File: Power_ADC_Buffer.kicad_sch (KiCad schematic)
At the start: 36 parts, among them U6 TLV6001DCK, U7 TLV6001DCK, U8 TLV6001DCK, U9 TLV6001DCK

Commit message: Adjusted cap sizes, 0603 for all need hand soldering, 0402 where possible, 0804 as needed
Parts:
- C20, C21, C22, C23, C24, C25, C26, C27: footprint Capacitor_SMD:C_0402_1005Metric_Pad0.74x0.62mm_HandSolder -> Capacitor_SMD:C_0603_1608Metric
- R12, R13, R14, R15, R16, R17, R18, R19, R20, R21, R22, R23, R24, R25, R26, R27, R28, R29, R30, R31: footprint Resistor_SMD:R_0402_1005Metric_Pad0.72x0.64mm_HandSolder -> Resistor_SMD:R_0603_1608Metric

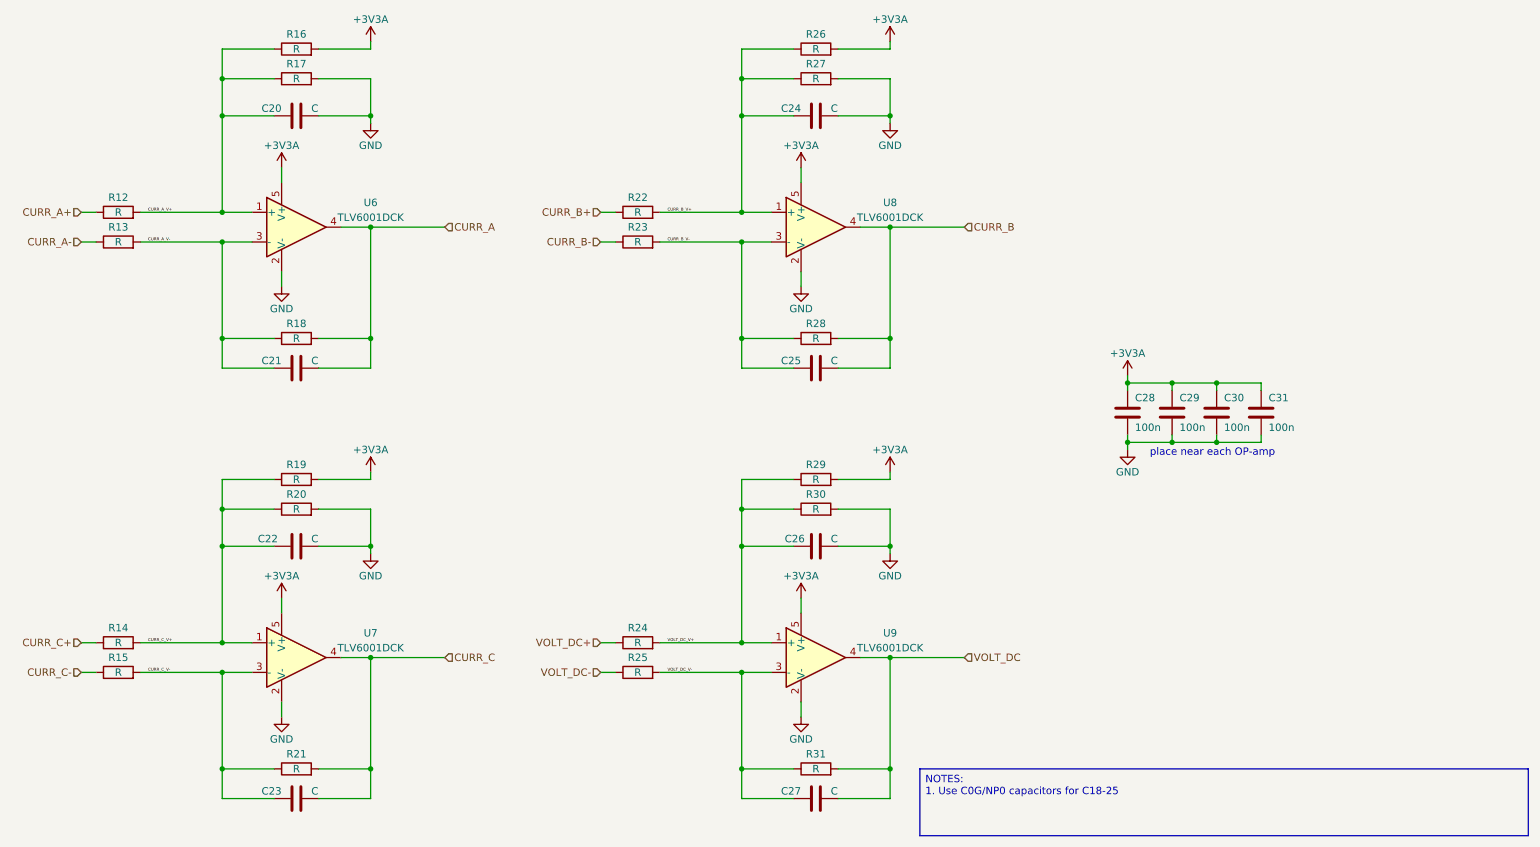
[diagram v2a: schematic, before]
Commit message: Changed op Amp, need to reroute, need to re-asses capacitor situation since || 0.1 and 1 is dumb. Just use 2 1s in that case.
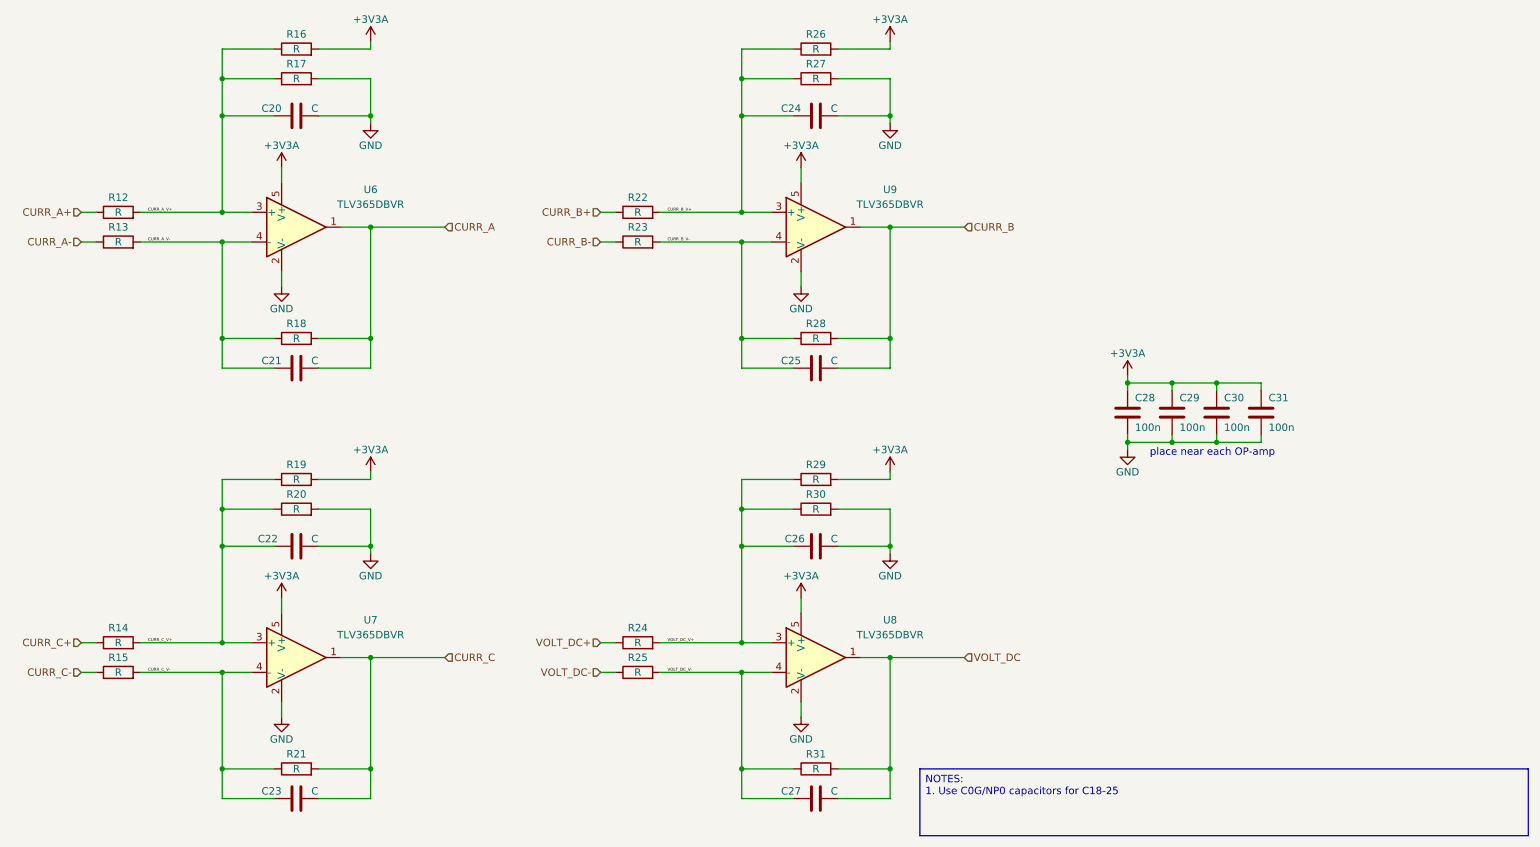
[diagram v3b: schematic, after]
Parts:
- removed U6, U7, U8, U9: TLV6001DCK, Package_TO_SOT_SMD:SOT-353_SC-70-5, symbol Amplifier_Operational:TLV6001DCK
- added U6, U7, U8, U9: TLV365DBVR, Package_TO_SOT_SMD:SOT-23-5, symbol User_OpAmp:TLV365DBVR
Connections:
- net +3V3A: now also U6.5 (V+), U7.5 (V+), U8.5 (V+), U9.5 (V+)
- net CURR_A: now also U6.1
- net CURR_A_V+: now also U6.3 (+)
- net CURR_A_V-: now also U6.4 (-)
- net CURR_B: now also U9.1
- net CURR_B_V+: now also U9.3 (+)
- net CURR_B_V-: now also U9.4 (-)
- net CURR_C: now also U7.1
- net CURR_C_V+: now also U7.3 (+)
- net CURR_C_V-: now also U7.4 (-)
- net GND: now also U6.2 (V-), U7.2 (V-), U8.2 (V-), U9.2 (V-)
- net VOLT_DC: now also U8.1
- net VOLT_DC_V+: now also U8.3 (+)
- net VOLT_DC_V-: now also U8.4 (-)

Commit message: Cheaper, smaller 10MHz Op Amp
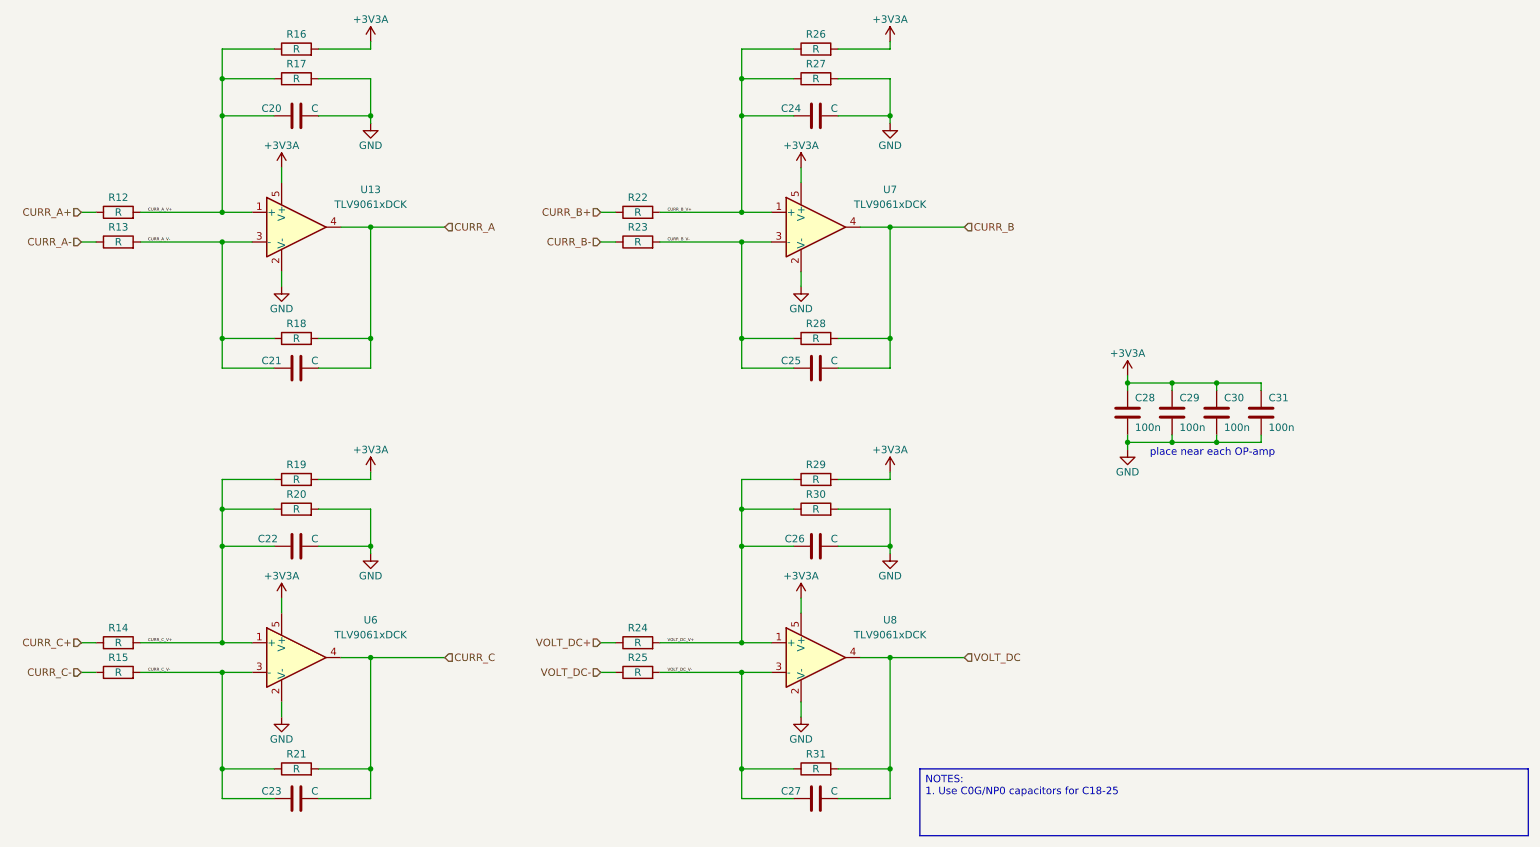
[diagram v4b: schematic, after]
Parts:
- removed U6, U7, U8, U9: TLV365DBVR, Package_TO_SOT_SMD:SOT-23-5, symbol User_OpAmp:TLV365DBVR
- added U13, U6, U7, U8: TLV9061xDCK, Package_TO_SOT_SMD:SOT-353_SC-70-5, symbol Amplifier_Operational:TLV9061xDCK
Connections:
- net +3V3A: now also U13.5 (V+), U6.5 (V+), U7.5 (V+), U8.5 (V+)
- net CURR_A: now also U13.4
- net CURR_A_V+: now also U13.1 (+)
- net CURR_A_V-: now also U13.3 (-)
- net CURR_B: now also U7.4
- net CURR_B_V+: now also U7.1 (+)
- net CURR_B_V-: now also U7.3 (-)
- net CURR_C: now also U6.4
- net CURR_C_V+: now also U6.1 (+)
- net CURR_C_V-: now also U6.3 (-)
- net GND: now also U13.2 (V-), U6.2 (V-), U7.2 (V-), U8.2 (V-)
- net VOLT_DC: now also U8.4
- net VOLT_DC_V+: now also U8.1 (+)
- net VOLT_DC_V-: now also U8.3 (-)

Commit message: Updating all decoupling to 1u
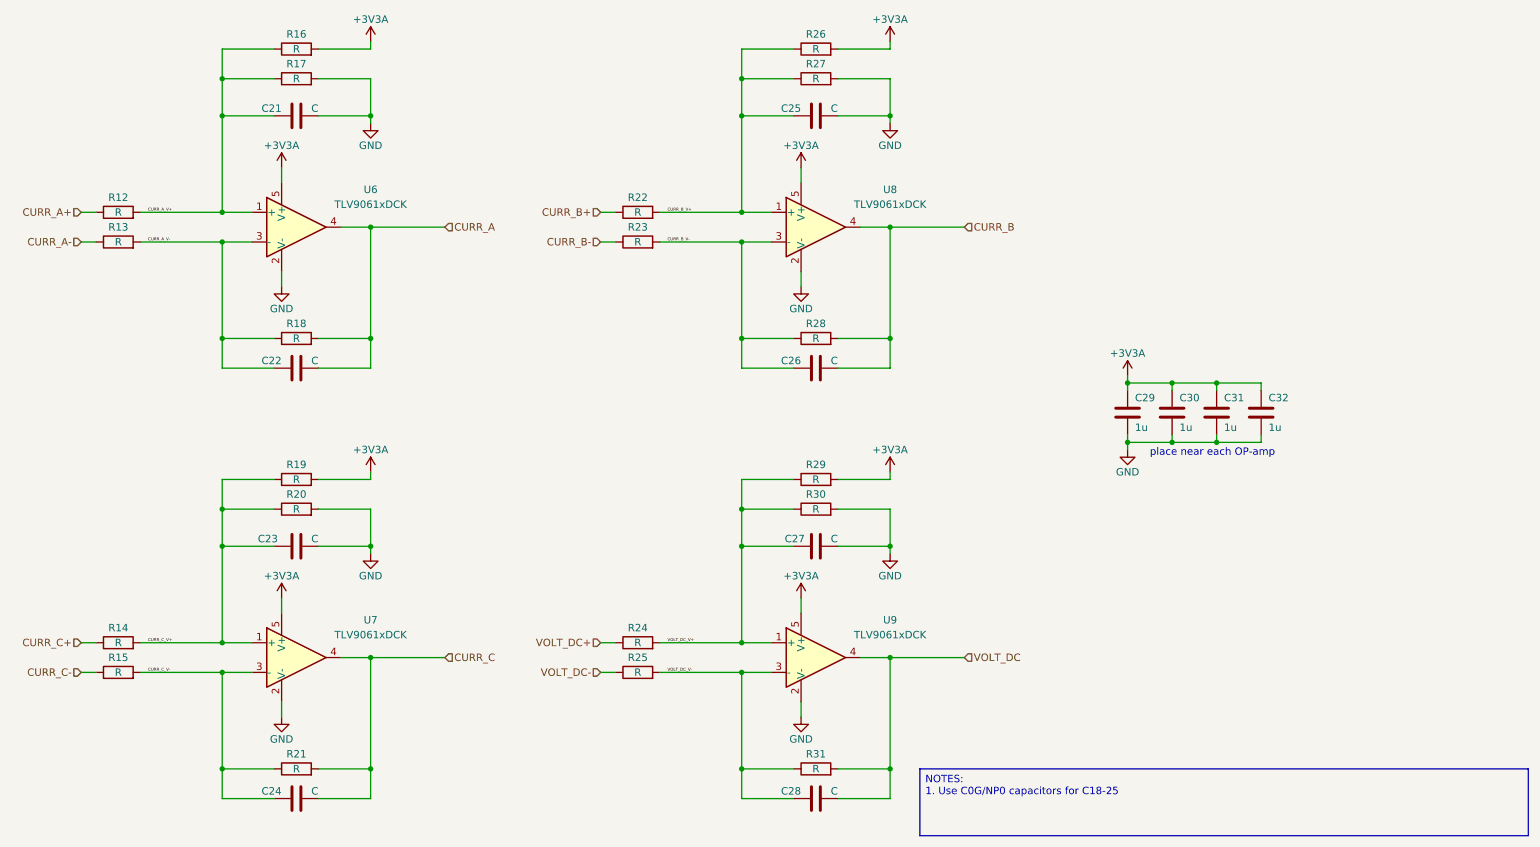
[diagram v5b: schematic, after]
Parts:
- removed C29: 100n, Capacitor_SMD:C_0402_1005Metric, symbol Device:C
- added C32: 1u, Capacitor_SMD:C_0402_1005Metric, symbol Device:C
- C29: renamed from C28; value 100n -> 1u
- C30, C31: value 100n -> 1u
- renumbered C20 to C21, C21 to C22, C22 to C23, C23 to C24, C24 to C25, C25 to C26, C26 to C27, C27 to C28, U13 to U6, U6 to U7, U7 to U8, U8 to U9
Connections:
- net +3V3A: now also C32.1
- net GND: now also C32.2
